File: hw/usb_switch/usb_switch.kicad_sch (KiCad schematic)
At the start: 30 parts, among them J1 USB_C_Receptacle_USB2.0, J2 USB_C_Receptacle_USB2.0, J3 Conn_01x02, J4 Conn_01x02, J5 Conn_01x02, J6 Conn_01x02, J7 USB_A, J8 USB_C_Receptacle_USB2.0, U1 MIC5504-3.3YM5, U2 FSUSB30L10X

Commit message: Updating footprints
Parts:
- C1, C2, C4, C5: footprint (none) -> Capacitor_SMD:C_0402_1005Metric
- C3: footprint (none) -> Capacitor_SMD:C_0805_2012Metric
- FB1, FB2, FB3, FB4: footprint (none) -> Inductor_SMD:L_0603_1608Metric
- J1, J2, J8: footprint (none) -> alvarop:USB4105-GF-A
- J3, J4, J5, J6: footprint (none) -> Connector_PinSocket_2.54mm:PinSocket_1x02_P2.54mm_Vertical
- R1, R10, R2, R3, R4, R5, R6, R7, R8, R9: footprint (none) -> Resistor_SMD:R_0402_1005Metric
- U2: footprint MICROPAK10_2P1X1P6_ONS -> (none)

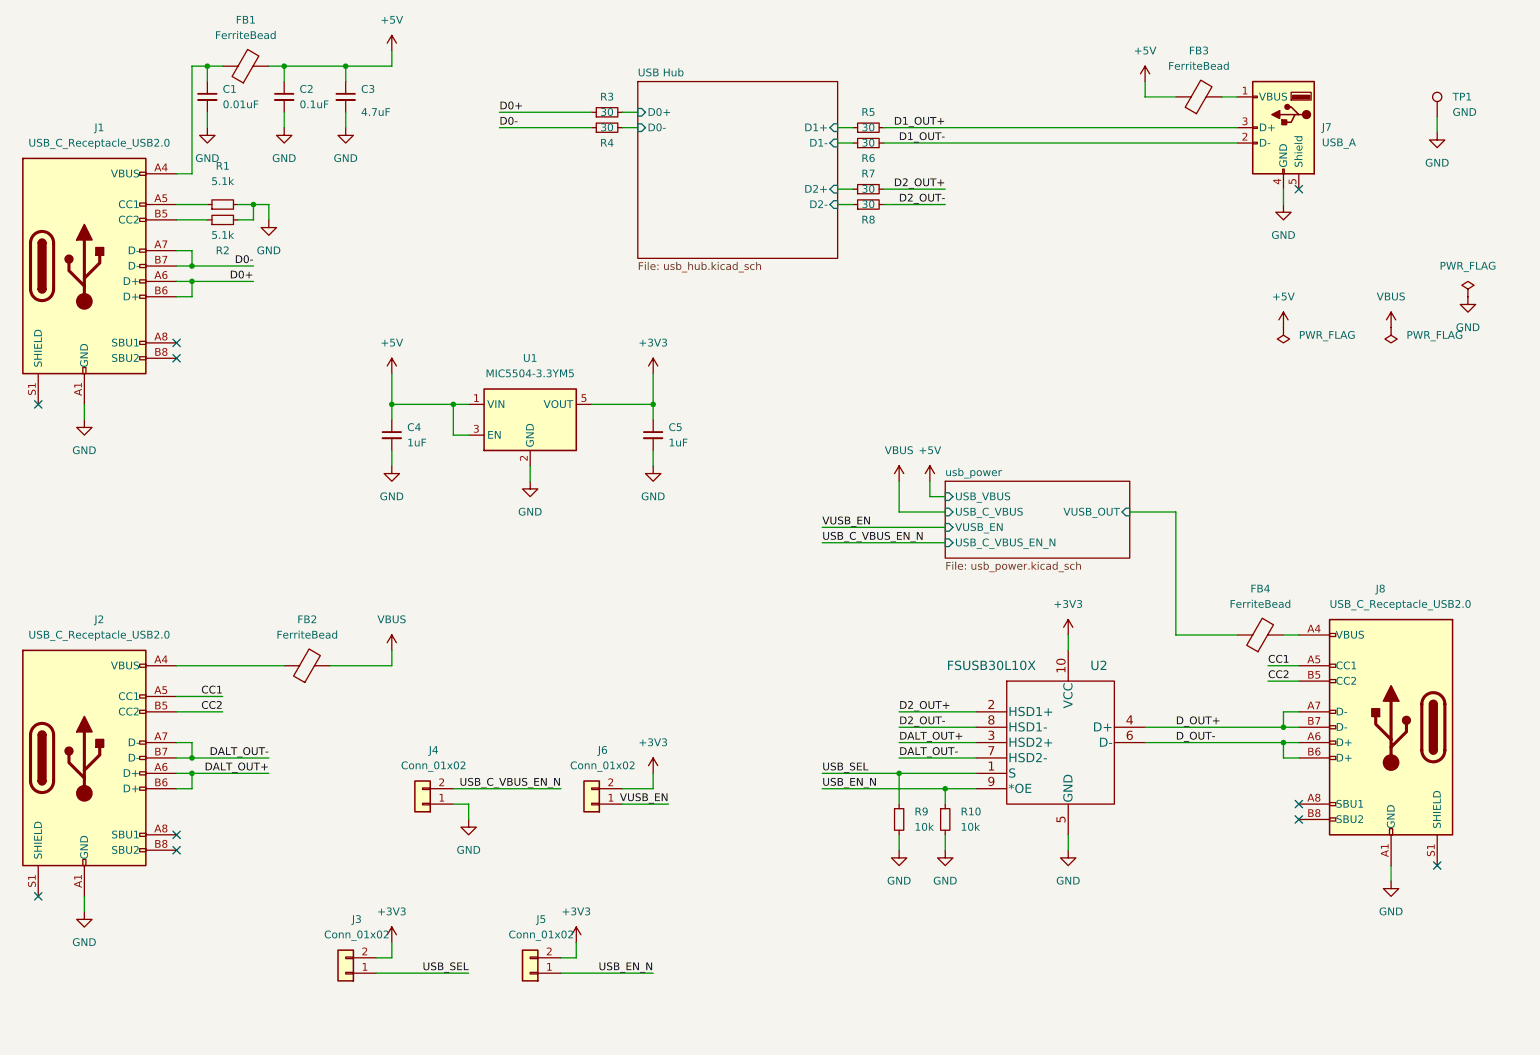
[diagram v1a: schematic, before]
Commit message: Some part changes and started layout
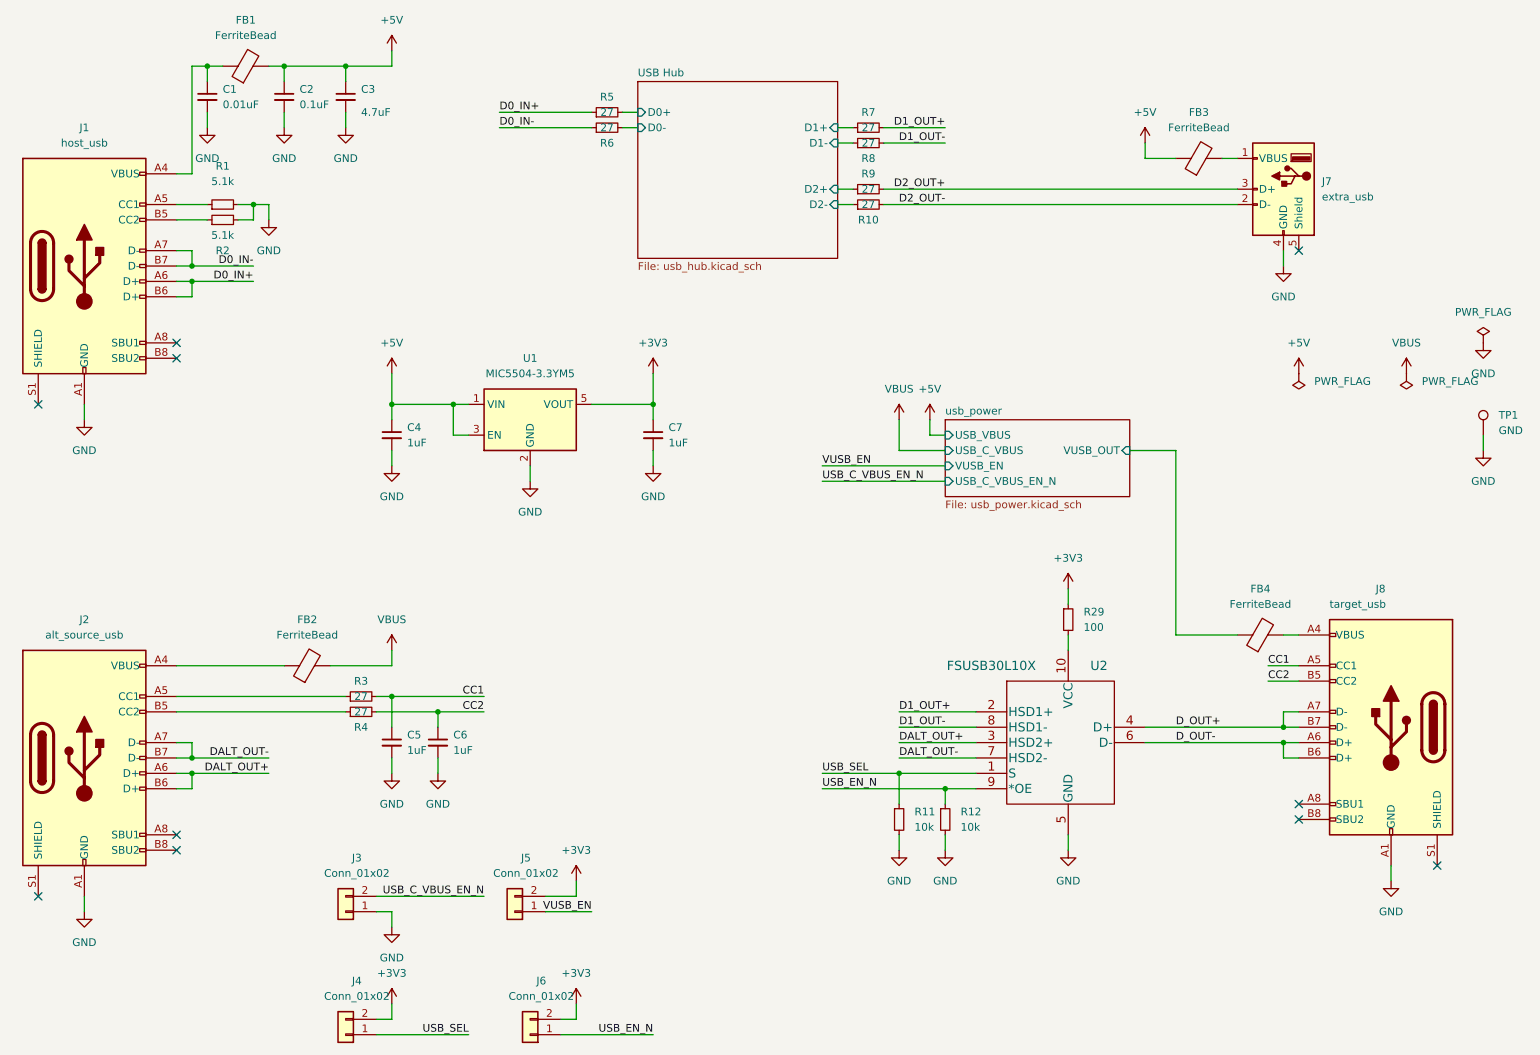
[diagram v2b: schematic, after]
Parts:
- added C5, C6: 1uF, Capacitor_SMD:C_0402_1005Metric, symbol Device:C_Small
- added R29: 100, Resistor_SMD:R_0402_1005Metric, symbol Device:R_Small
- added R3, R4: 27, Resistor_SMD:R_0402_1005Metric, symbol Device:R_Small
- J1: value USB_C_Receptacle_USB2.0 -> host_usb
- J2: value USB_C_Receptacle_USB2.0 -> alt_source_usb
- J7: value USB_A -> extra_usb; footprint (none) -> alvarop:UE27ACX410X
- J8: value USB_C_Receptacle_USB2.0 -> target_usb
- R10: renamed from R8; value 30 -> 27
- R5: renamed from R3; value 30 -> 27
- R6: renamed from R4; value 30 -> 27
- R7: renamed from R5; value 30 -> 27
- R8: renamed from R6; value 30 -> 27
- R9: renamed from R7; value 30 -> 27
- TP1: footprint (none) -> alvarop:RCWCTE
- U2: footprint (none) -> Package_SO:MSOP-10_3x3mm_P0.5mm
- renumbered C5 to C7, J4 to J3, J3 to J4, J6 to J5, J5 to J6, R9 to R11, R10 to R12
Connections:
- net +3V3: now also R29.1; no longer U2.10 (VCC)
- net CC1: now also C5.1, R3.2; no longer J2.A5 (CC1)
- net CC2: now also C6.1, R4.2; no longer J2.B5 (CC2)
- net D1_OUT+: now also U2.2 (HSD1+); no longer J7.3 (D+)
- net D1_OUT-: now also U2.8 (HSD1-); no longer J7.2 (D-)
- net D2_OUT+: now also J7.3 (D+); no longer U2.2 (HSD1+)
- net D2_OUT-: now also J7.2 (D-); no longer U2.8 (HSD1-)
- net GND: now also C5.2, C6.2
- net D0+ renamed D0_IN+
- net D0- renamed D0_IN-
- new net: J2.A5 (CC1), R3.1
- new net: J2.B5 (CC2), R4.1
- new net: R29.2, U2.10 (VCC)
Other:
- moved on the sheet: FB3, J3, J4, J5, J6, J7, TP1

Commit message: Finished and ordered from JLCPCB!
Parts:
- added C22: 0.1uF, Capacitor_SMD:C_0402_1005Metric, symbol Device:C_Small
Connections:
- net GND: now also C22.2
- net at R29.2, U2.10 (VCC): now also C22.1
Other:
- note added: "From FSUSB30L10X datasheet: The USB 2.0 specification notes that the USB device should be capable of withstanding a Vbus short during transmission of data. Fairchild recommends adding a 100 series resistor between the switch VCC pin and supply rail to protect against this case. This modification works by limiting current flow back into the VCC rail during the over-voltage event so current remains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"
- moved on the sheet: R11, R12, R29, U2

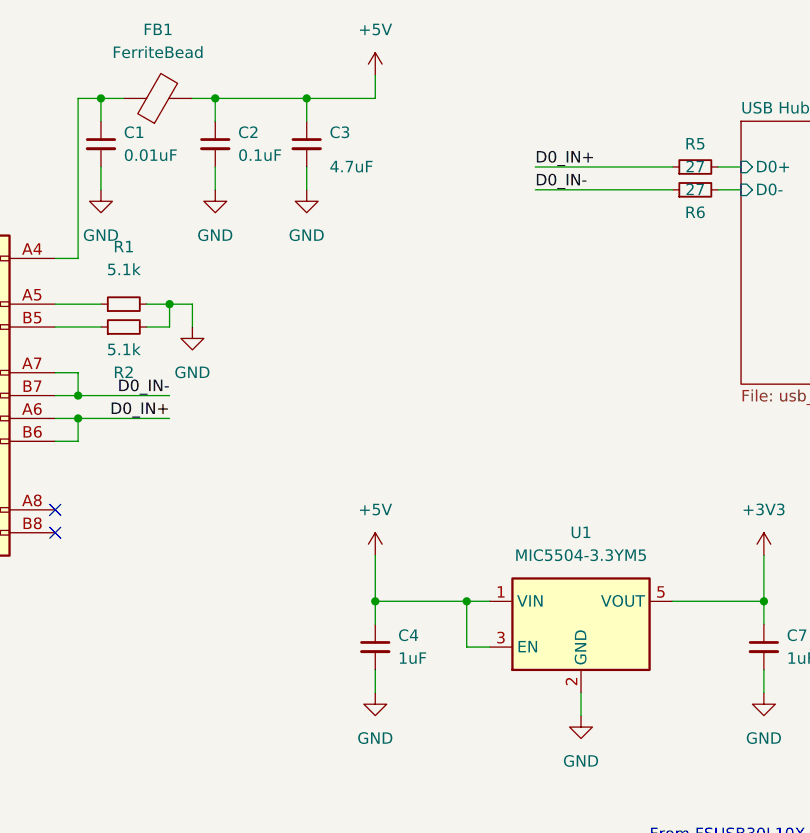
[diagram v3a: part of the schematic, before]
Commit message: Added MPNs and values to usb_switch
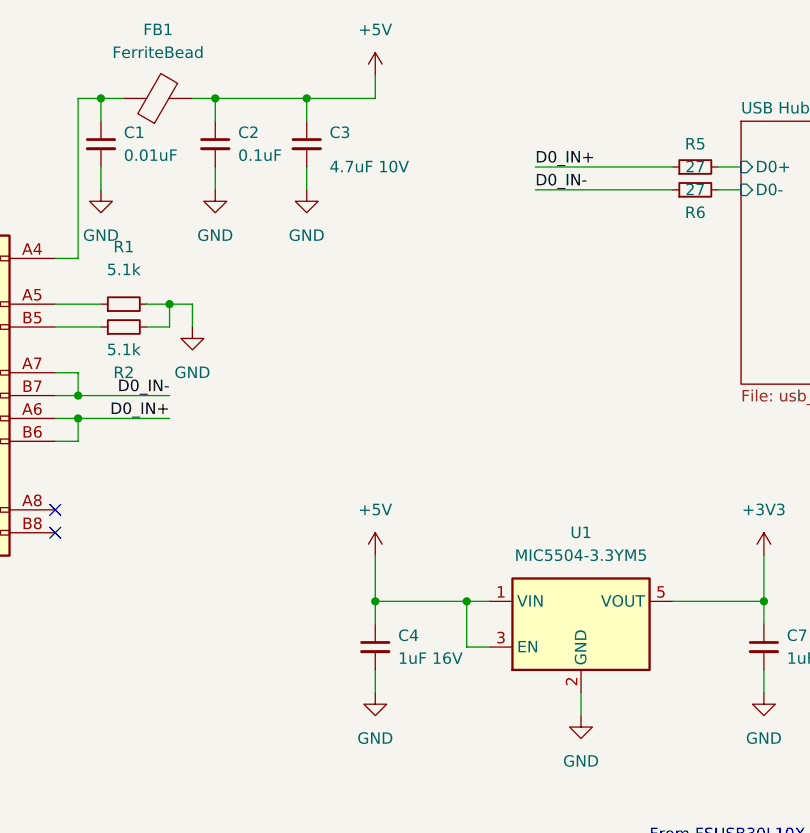
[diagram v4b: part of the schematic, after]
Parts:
- C3: value 4.7uF -> 4.7uF 10V
- C4: value 1uF -> 1uF 16V
- FB1, FB2, FB3, FB4: MPN (none) -> FBMJ1608HS280NTR
- J1, J2, J8: MPN (none) -> USB4105-GF-A
- J7: MPN (none) -> UE27AC54100
- TP1: MPN (none) -> RCWCTE
- U1: MPN (none) -> MIC5504-3.3YM5-TR
- U2: MPN (none) -> FSUSB30L10X
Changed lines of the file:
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@@
+      (effects (font (size 1.27 1.27)) hide)
+    )
+    (property "MPN" "FBMJ1608HS280NTR" (id 4) (at 80.01 124.46 0)
       (effects (font (size 1.27 1.27)) hide)
     )
@@
       (effects (font (size 1.27 1.27)) hide)
     )
+    (property "MPN" "FBMJ1608HS280NTR" (id 4) (at 227.33 40.64 0)
+      (effects (font (size 1.27 1.27)) hide)
+    )
     (pin "1")
     (pin "2")
@@
     )
     (property "Datasheet" "https://www.usb.org/sites/default/files/documents/usb_type-c.zip" (id 3) (at 46.99 139.7 0)
+      (effects (font (size 1.27 1.27)) hide)
+    )
+    (property "MPN" "USB4105-GF-A" (id 4) (at 43.18 139.7 0)
       (effects (font (size 1.27 1.27)) hide)
     )
@@
       (effects (font (size 1.27 1.27)) hide)
     )
+    (property "MPN" "USB4105-GF-A" (id 4) (at 43.18 58.42 0)
+      (effects (font (size 1.27 1.27)) hide)
+    )
     (pin "A1")
     (pin "A12")
@@
       (effects (font (size 1.27 1.27)) hide)
     )
+    (property "MPN" "RCWCTE" (id 4) (at 274.32 86.36 0)
+      (effects (font (size 1.27 1.27)) hide)
+    )
     (pin "1")
   )
@@
       (effects (font (size 1.27 1.27)) hide)
     )
+    (property "MPN" "UE27AC54100" (id 4) (at 241.3 45.72 0)
+      (effects (font (size 1.27 1.27)) hide)
+    )
     (pin "1")
     (pin "2")
@@
     )
     (property "Datasheet" "https://www.usb.org/sites/default/files/documents/usb_type-c.zip" (id 3) (at 255.27 134.62 0)
+      (effects (font (size 1.27 1.27)) hide)
+    )
+    (property "MPN" "USB4105-GF-A" (id 4) (at 259.08 134.62 0)
       (effects (font (size 1.27 1.27)) hide)
     )
@@
       (effects (font (size 1.27 1.27)) hide)
     )
+    (property "MPN" "MIC5504-3.3YM5-TR" (id 4) (at 116.84 83.82 0)
+      (effects (font (size 1.27 1.27)) hide)
+    )
     (pin "1")
     (pin "2")
@@
       (effects (font (size 1.27 1.27)) (justify left))
     )
-    (property "Value" "4.7uF" (id 1) (at 88.9 33.02 0)
+    (property "Value" "4.7uF 10V" (id 1) (at 88.9 33.02 0)
       (effects (font (size 1.27 1.27)) (justify left))
     )
@@
   (symbol (lib_id "Device:C_Small") (at 93.98 86.36 0) (unit 1)
     (in_bom yes) (on_board yes) (fields_autoplaced)
-    (property "Reference" "C4" (id 0) (at 96.52 85.0899 0)
-      (effects (font (size 1.27 1.27)) (justify left))
-    )
-    (property "Value" "1uF" (id 1) (at 96.52 87.6299 0)
+    (property "Reference" "C4" (id 0) (at 96.52 85.0962 0)
+      (effects (font (size 1.27 1.27)) (justify left))
+    )
+    (property "Value" "1uF 16V" (id 1) (at 96.52 87.6362 0)
       (effects (font (size 1.27 1.27)) (justify left))
     )
@@
     (property "Datasheet" "" (id 3) (at 210.82 121.92 0)
       (effects (font (size 1.524 1.524)))
+    )
+    (property "MPN" "FSUSB30L10X" (id 4) (at 210.82 137.16 0)
+      (effects (font (size 1.27 1.27)) hide)
     )
     (pin "1")
@@
       (effects (font (size 1.27 1.27)) hide)
     )
+    (property "MPN" "FBMJ1608HS280NTR" (id 4) (at 237.49 119.38 0)
+      (effects (font (size 1.27 1.27)) hide)
+    )
     (pin "1")
     (pin "2")
@@
       (effects (font (size 1.27 1.27)) hide)
     )
+    (property "MPN" "FBMJ1608HS280NTR" (id 4) (at 69.85 25.4 0)
+      (effects (font (size 1.27 1.27)) hide)
+    )
     (pin "1")
     (pin "2")
@@
     )
     (path "/a42c254f-8c2e-421e-9061-40b3392cc167"
-      (reference "C3") (unit 1) (value "4.7uF") (footprint "Capacitor_SMD:C_0805_2012Metric")
+      (reference "C3") (unit 1) (value "4.7uF 10V") (footprint "Capacitor_SMD:C_0805_2012Metric")
     )
     (path "/ccf446da-47d5-47a0-855b-2c6c36b5858c"
-      (reference "C4") (unit 1) (value "1uF") (footprint "Capacitor_SMD:C_0402_1005Metric")
+      (reference "C4") (unit 1) (value "1uF 16V") (footprint "Capacitor_SMD:C_0402_1005Metric")
     )
     (path "/b523d498-3e73-4ef7-8a7c-42b8f93a7e63"
@@
     )
     (path "/5e5251fb-5746-4f50-9b0e-0dd04aa6b340/95190bb4-1507-461d-9d7b-d82eed8714fc"
-      (reference "C14") (unit 1) (value "1uF") (footprint "Capacitor_SMD:C_0402_1005Metric")
+      (reference "C14") (unit 1) (value "1uF 16V") (footprint "Capacitor_SMD:C_0402_1005Metric")
     )
     (path "/5e5251fb-5746-4f50-9b0e-0dd04aa6b340/82159412-1d76-4c5b-8b8c-33644a0462a6"
@@
     )
     (path "/5e5251fb-5746-4f50-9b0e-0dd04aa6b340/29ae3363-1a08-452b-8673-20d0513a0e5b"
-      (reference "C16") (unit 1) (value "1uF") (footprint "Capacitor_SMD:C_0402_1005Metric")
+      (reference "C16") (unit 1) (value "1uF 35V") (footprint "Capacitor_SMD:C_0402_1005Metric")
     )
     (path "/5e5251fb-5746-4f50-9b0e-0dd04aa6b340/a155e72b-73c8-49d6-b07a-0fe76ab47539"
-      (reference "C17") (unit 1) (value "1uF") (footprint "Capacitor_SMD:C_0402_1005Metric")
+      (reference "C17") (unit 1) (value "1uF 16V") (footprint "Capacitor_SMD:C_0402_1005Metric")
     )
     (path "/5e5251fb-5746-4f50-9b0e-0dd04aa6b340/68658c7f-2d2a-42cb-abac-a46a0bdd30b9"
-      (reference "C18") (unit 1) (value "10uF") (footprint "Capacitor_SMD:C_0603_1608Metric")
+      (reference "C18") (unit 1) (value "10uF 10V") (footprint "Capacitor_SMD:C_0603_1608Metric")
     )
     (path "/5e5251fb-5746-4f50-9b0e-0dd04aa6b340/17ab743d-2983-40b0-a261-a79f502d20da"
-      (reference "C19") (unit 1) (value "C_Small") (footprint "Capacitor_SMD:C_0402_1005Metric")
+      (reference "C19") (unit 1) (value "0.01uF") (footprint "Capacitor_SMD:C_0402_1005Metric")
     )
     (path "/5e5251fb-5746-4f50-9b0e-0dd04aa6b340/6d527468-5566-4e4d-b1eb-98e76b38cdd0"
-      (reference "C20") (unit 1) (value "1uF") (footprint "Capacitor_SMD:C_0402_1005Metric")
+      (reference "C20") (unit 1) (value "1uF 35V") (footprint "Capacitor_SMD:C_0402_1005Metric")
     )
     (path "/5e5251fb-5746-4f50-9b0e-0dd04aa6b340/c7b7968a-fbd1-4a56-b3e5-6f21ba502a5b"
-      (reference "C21") (unit 1) (value "22uF") (footprint "Capacitor_SMD:C_0805_2012Metric")
+      (reference "C21") (unit 1) (value "22uF 25V") (footprint "Capacitor_SMD:C_0805_2012Metric")
     )
     (path "/cd06e7ea-609a-4497-8932-f50a53b6711e"
